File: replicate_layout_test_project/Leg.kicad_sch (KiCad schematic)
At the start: 8 parts, among them Q501 CSD19531KCS, Q502 CSD19531KCS, U501 IR2181

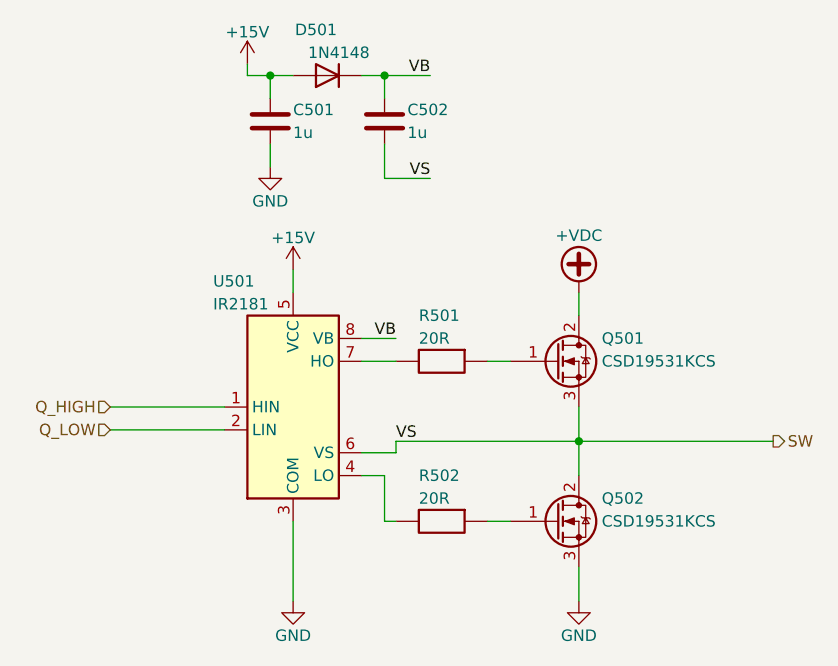
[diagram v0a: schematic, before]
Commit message: Improve error messages that user sees
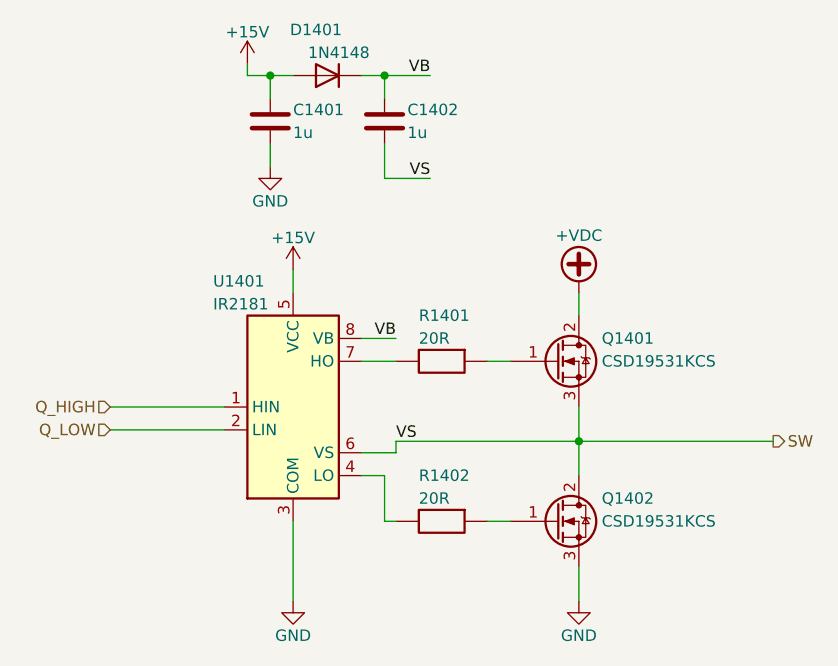
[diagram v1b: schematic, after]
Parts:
- renumbered C501 to C1401, C502 to C1402, D501 to D1401, Q501 to Q1401, Q502 to Q1402, R501 to R1401, R502 to R1402, U501 to U1401
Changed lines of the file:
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@@
     (effects (font (size 1.27 1.27)) (justify right))
   )
-  (symbol (lib_id "Diode:1N4148") (at 99.06 43.18 180)
-    (in_bom yes) (on_board yes)
-    (property "Reference" "D501" (id 0) (at 97.79 38.1 0))
+  (symbol (lib_id "Diode:1N4148") (at 99.06 43.18 180) (unit 1)
+    (in_bom yes) (on_board yes)
+    (property "Reference" "D1401" (id 0) (at 97.79 38.1 0))
     (property "Value" "1N4148" (id 1) (at 100.33 40.64 0))
     (property "Footprint" "Diode_SMD:D_MiniMELF" (id 2) (at 99.06 38.735 0)
@@
     (pin "2")
   )
-  (symbol (lib_id "Discretes:CSD19531KCS") (at 124.46 74.93 0)
-    (in_bom yes) (on_board yes)
-    (property "Reference" "Q501" (id 0) (at 129.54 72.39 0)
+  (symbol (lib_id "Discretes:CSD19531KCS") (at 124.46 74.93 0) (unit 1)
+    (in_bom yes) (on_board yes)
+    (property "Reference" "Q1401" (id 0) (at 129.54 72.39 0)
       (effects (font (size 1.27 1.27)) (justify left))
     )
@@
     (pin "3")
   )
-  (symbol (lib_id "power:GND") (at 92.71 53.34 0)
-    (in_bom yes) (on_board yes)
-    (property "Reference" "#PWR0502" (id 0) (at 92.71 59.69 0)
+  (symbol (lib_id "power:GND") (at 92.71 53.34 0) (unit 1)
+    (in_bom yes) (on_board yes)
+    (property "Reference" "#PWR01402" (id 0) (at 92.71 59.69 0)
       (effects (font (size 1.27 1.27)) hide)
     )
@@
     (pin "1")
   )
-  (symbol (lib_id "power:+15V") (at 90.17 41.91 0)
-    (in_bom yes) (on_board yes)
-    (property "Reference" "#PWR0501" (id 0) (at 90.17 45.72 0)
+  (symbol (lib_id "power:+15V") (at 90.17 41.91 0) (unit 1)
+    (in_bom yes) (on_board yes)
+    (property "Reference" "#PWR01401" (id 0) (at 90.17 45.72 0)
       (effects (font (size 1.27 1.27)) hide)
     )
@@
     (pin "1")
   )
-  (symbol (lib_id "power:GND") (at 95.25 101.6 0)
-    (in_bom yes) (on_board yes)
-    (property "Reference" "#PWR0504" (id 0) (at 95.25 107.95 0)
+  (symbol (lib_id "power:GND") (at 95.25 101.6 0) (unit 1)
+    (in_bom yes) (on_board yes)
+    (property "Reference" "#PWR01404" (id 0) (at 95.25 107.95 0)
       (effects (font (size 1.27 1.27)) hide)
     )
@@
     (pin "1")
   )
-  (symbol (lib_id "Passives:R1206") (at 111.76 92.71 0)
-    (in_bom yes) (on_board yes)
-    (property "Reference" "R502" (id 0) (at 109.22 87.63 0)
+  (symbol (lib_id "Passives:R1206") (at 111.76 92.71 0) (unit 1)
+    (in_bom yes) (on_board yes)
+    (property "Reference" "R1402" (id 0) (at 109.22 87.63 0)
       (effects (font (size 1.27 1.27)) (justify left))
     )
@@
     (pin "2")
   )
-  (symbol (lib_id "Discretes:CSD19531KCS") (at 124.46 92.71 0)
-    (in_bom yes) (on_board yes)
-    (property "Reference" "Q502" (id 0) (at 129.54 90.17 0)
+  (symbol (lib_id "Discretes:CSD19531KCS") (at 124.46 92.71 0) (unit 1)
+    (in_bom yes) (on_board yes)
+    (property "Reference" "Q1402" (id 0) (at 129.54 90.17 0)
       (effects (font (size 1.27 1.27)) (justify left))
     )
@@
     (pin "3")
   )
-  (symbol (lib_id "power:+VDC") (at 127 67.31 0)
-    (in_bom yes) (on_board yes)
-    (property "Reference" "#PWR0505" (id 0) (at 127 69.85 0)
+  (symbol (lib_id "power:+VDC") (at 127 67.31 0) (unit 1)
+    (in_bom yes) (on_board yes)
+    (property "Reference" "#PWR01405" (id 0) (at 127 69.85 0)
       (effects (font (size 1.27 1.27)) hide)
     )
@@
     (pin "1")
   )
-  (symbol (lib_id "power:GND") (at 127 101.6 0)
-    (in_bom yes) (on_board yes)
-    (property "Reference" "#PWR0506" (id 0) (at 127 107.95 0)
+  (symbol (lib_id "power:GND") (at 127 101.6 0) (unit 1)
+    (in_bom yes) (on_board yes)
+    (property "Reference" "#PWR01406" (id 0) (at 127 107.95 0)
       (effects (font (size 1.27 1.27)) hide)
     )
@@
     (pin "1")
   )
-  (symbol (lib_id "power:+15V") (at 95.25 64.77 0)
-    (in_bom yes) (on_board yes)
-    (property "Reference" "#PWR0503" (id 0) (at 95.25 68.58 0)
+  (symbol (lib_id "power:+15V") (at 95.25 64.77 0) (unit 1)
+    (in_bom yes) (on_board yes)
+    (property "Reference" "#PWR01403" (id 0) (at 95.25 68.58 0)
       (effects (font (size 1.27 1.27)) hide)
     )
@@
     (pin "1")
   )
-  (symbol (lib_id "Passives:C1206") (at 92.71 48.26 0)
-    (in_bom yes) (on_board yes)
-    (property "Reference" "C501" (id 0) (at 95.25 46.99 0)
+  (symbol (lib_id "Passives:C1206") (at 92.71 48.26 0) (unit 1)
+    (in_bom yes) (on_board yes)
+    (property "Reference" "C1401" (id 0) (at 95.25 46.99 0)
       (effects (font (size 1.27 1.27)) (justify left))
     )
@@
     (pin "2")
   )
-  (symbol (lib_id "Passives:R1206") (at 111.76 74.93 0)
-    (in_bom yes) (on_board yes)
-    (property "Reference" "R501" (id 0) (at 109.22 69.85 0)
+  (symbol (lib_id "Passives:R1206") (at 111.76 74.93 0) (unit 1)
+    (in_bom yes) (on_board yes)
+    (property "Reference" "R1401" (id 0) (at 109.22 69.85 0)
       (effects (font (size 1.27 1.27)) (justify left))
     )
@@
     (pin "2")
   )
-  (symbol (lib_id "Driver_FET:IR2181") (at 95.25 80.01 0)
-    (in_bom yes) (on_board yes)
-    (property "Reference" "U501" (id 0) (at 86.36 66.04 0)
+  (symbol (lib_id "Driver_FET:IR2181") (at 95.25 80.01 0) (unit 1)
+    (in_bom yes) (on_board yes)
+    (property "Reference" "U1401" (id 0) (at 86.36 66.04 0)
       (effects (font (size 1.27 1.27)) (justify left))
     )
@@
     (pin "8")
   )
-  (symbol (lib_id "Passives:C1206") (at 105.41 48.26 0)
-    (in_bom yes) (on_board yes)
-    (property "Reference" "C502" (id 0) (at 107.95 46.99 0)
-      (effects (font (size 1.27 1.27)) (justify left))
-    )
+  (symbol (lib_id "Passives:C1206") (at 105.41 48.26 0) (unit 1)
+    (in_bom yes) (on_board yes)
+    (property "Reference" "C1402" (id 0) (at 107.95 46.99 0)
+      (effects (font (size 1.27 1.27)) (justify left))
+    )
